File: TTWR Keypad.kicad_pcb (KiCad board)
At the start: 4 copper layers, 35.5 x 60 mm, 46 parts, among them J1 Conn_01x15, J2 Conn_01x15, U1 PTS526 SK15 SMTR2 LFS, U10 PTS526 SK15 SMTR2 LFS, U11 PTS526 SK15 SMTR2 LFS, U12 PTS526 SK15 SMTR2 LFS, U13 PTS526 SK15 SMTR2 LFS, U14 PTS526 SK15 SMTR2 LFS, U15 PTS526 SK15 SMTR2 LFS, U16 PTS526 SK15 SMTR2 LFS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

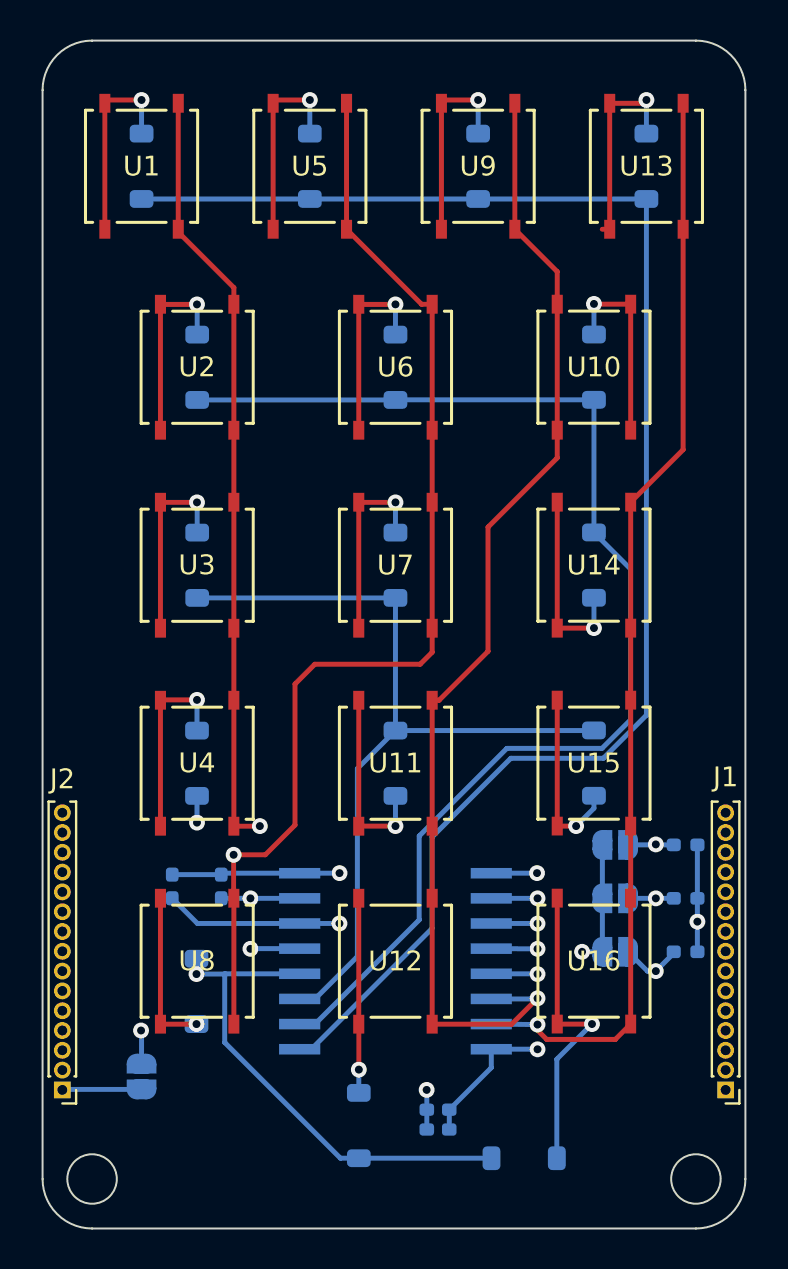
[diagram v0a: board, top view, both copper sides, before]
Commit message: Changed footprints of R* and C* to 0603 and made layout adjustments to compensate. Added JLCPCB metafiles for fab and population.
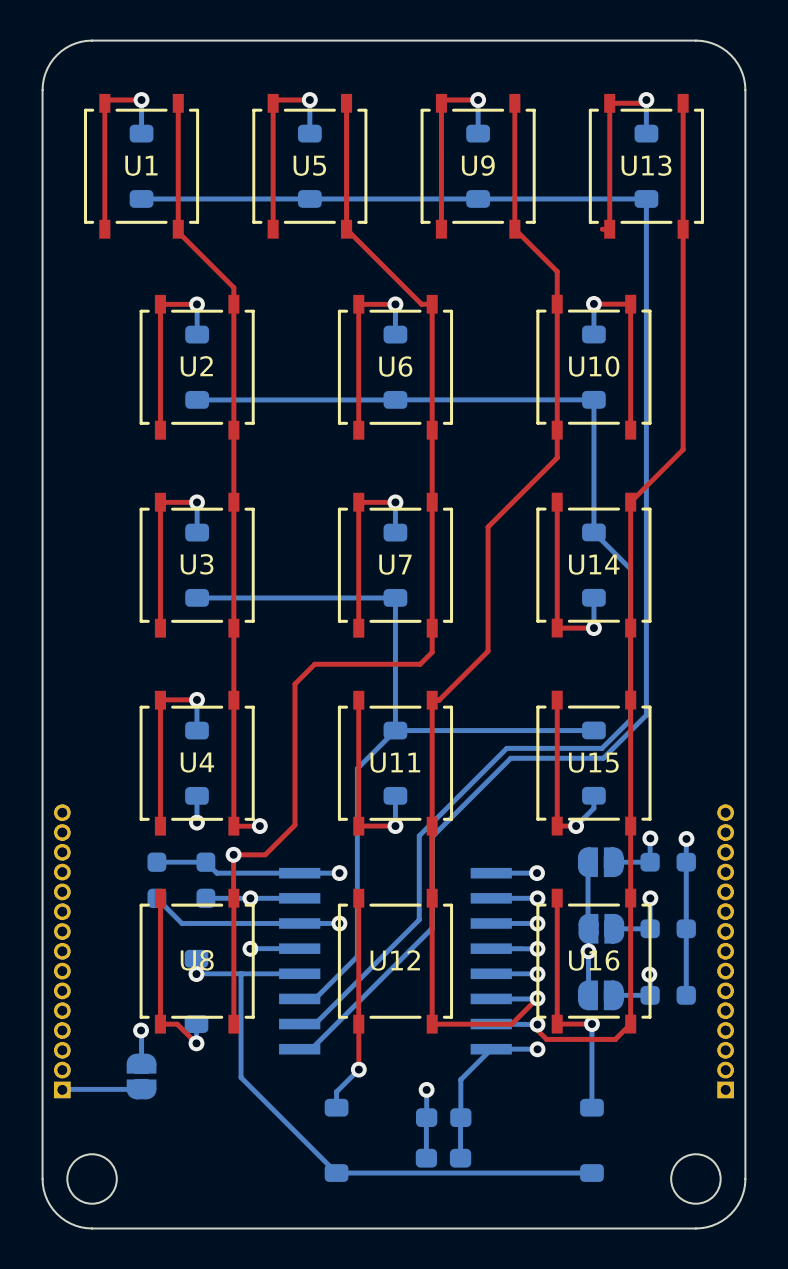
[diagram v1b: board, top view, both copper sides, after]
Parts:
- C1, C2: footprint Capacitor_SMD:C_0402_1005Metric_Pad0.74x0.62mm_HandSolder -> Capacitor_SMD:C_0603_1608Metric_Pad1.08x0.95mm_HandSolder
- J1, J2: moved to B.Cu
- R1, R2, R3, R4, R5: footprint Resistor_SMD:R_0402_1005Metric_Pad0.72x0.64mm_HandSolder -> Resistor_SMD:R_0603_1608Metric_Pad0.98x0.95mm_HandSolder
- moved D16 3.54 mm to (177.8, 95.5), turned to 90 degrees
- moved R5 2.37 mm to (181.6, 88.2)
- moved JP3 2.32 mm to (178.2, 88.2)
- moved R4 1.77 mm to (181.6, 84.9)
- moved JP2 1.69 mm to (178.2, 84.9)
- moved C2 1.48 mm to (170.2, 96.5)
- moved D12 1.35 mm to (164.8, 95.5)
- moved R3 1.24 mm to (181.6, 81.5)
- moved JP1 1.14 mm to (178.2, 81.5)
- moved R1 0.84 mm to (158.2, 82.4)
- moved R2 0.84 mm to (155.8, 82.4)
- moved C1 0.49 mm to (170.3, 94.4)
- turned J1 to 0 degrees
- turned J2 to 0 degrees
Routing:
- net GND: track 32.6 -> 16.4 mm
- net ROW_3: track 34.4 -> 40.0 mm
- net Net-(D16-A): track 15.6 -> 12.3 mm
- net +3.3V: track 52.2 -> 55.0 mm
- net Net-(D8-A): track 8.19 -> 9.56 mm
- net Net-(D12-A): track 9.83 -> 11.0 mm
- net /IO Expander/A1: track 10.7 -> 11.7 mm
- net /IO Expander/SDA: track 33.1 -> 33.9 mm
- net /IO Expander/SCL: track 34.7 -> 35.5 mm
- net /IO Expander/A2: track 12.5 -> 12.0 mm
- added copper zone on In1.Cu, net GND

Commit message: Added ground plane to second inner layer and regenerated gerber files.
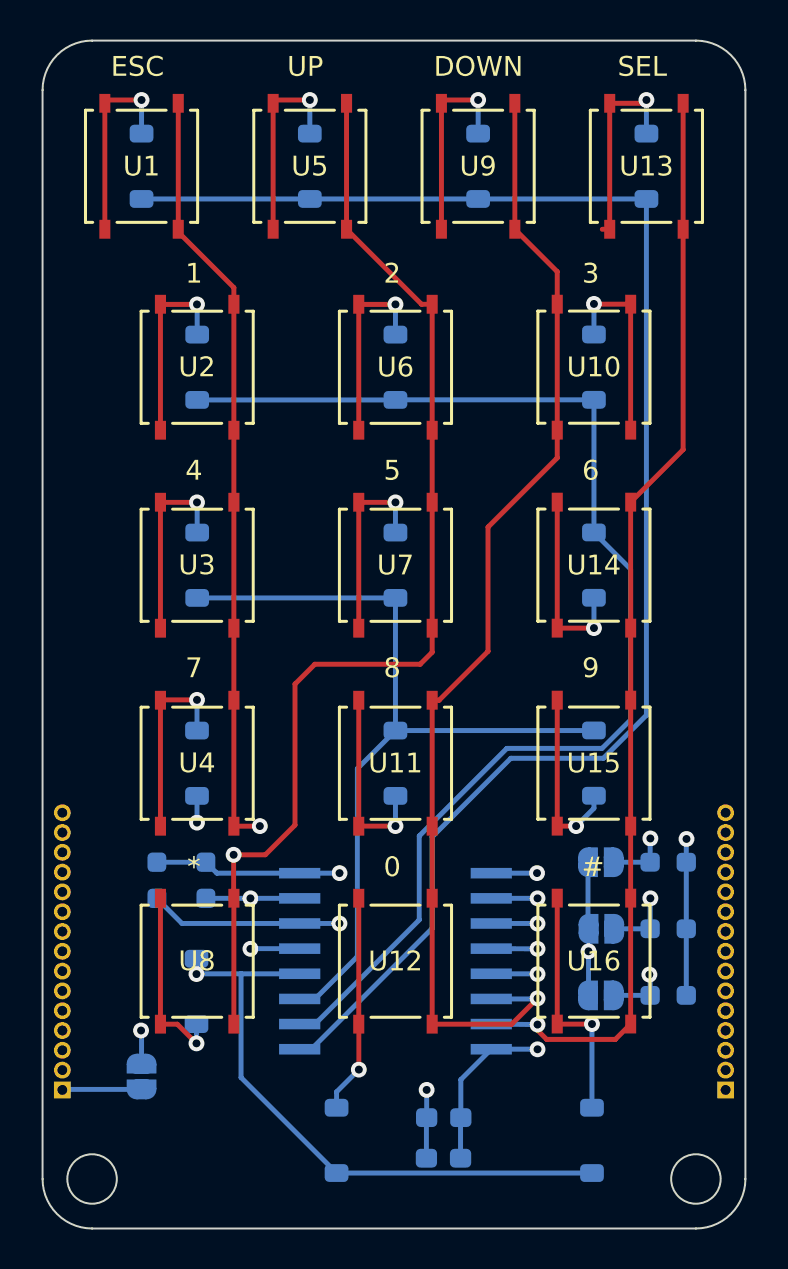
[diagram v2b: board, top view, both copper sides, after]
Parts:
- JP1: value SolderJumper_2_Open -> A0
- JP2: value SolderJumper_2_Open -> A1
- JP3: value SolderJumper_2_Open -> A2
- JP4: value SolderJumper_2_Open -> INT
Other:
- board text added: "#"
- board text added: "*"
- board text added: "0"
- board text added: "1"
- board text added: "2"
- board text added: "3"
- board text added: "4"
- board text added: "5"
- board text added: "6"
- board text added: "7"
- board text added: "8"
- board text added: "9"
- board text added: "DOWN"
- board text added: "ESC"
- board text added: "SEL"
- board text added: "UP"
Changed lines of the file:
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@@
 			(at 0 1.8 90)
 			(layer "B.SilkS")
+			(hide yes)
 			(effects
 				(font
@@
 			)
 		)
-		(property "Value" "SolderJumper_2_Open"
+		(property "Value" "INT"
 			(at 0 -1.9 90)
-			(layer "B.Fab")
-			(hide yes)
+			(layer "B.SilkS")
 			(effects
 				(font
@@
 		(sheetname "IO Expander")
 		(sheetfile "IO Expander.kicad_sch")
-		(attr exclude_from_pos_files)
+		(attr exclude_from_pos_files exclude_from_bom)
 		(fp_line
 			(start -0.7 1)
@@
 			(at -2.35 0 90)
 			(layer "B.SilkS")
+			(hide yes)
 			(effects
 				(font
@@
 			)
 		)
-		(property "Value" "SolderJumper_2_Open"
-			(at 0 -1.9 0)
-			(layer "B.Fab")
-			(hide yes)
+		(property "Value" "A2"
+			(at -2.325 0 -90)
+			(layer "B.SilkS")
 			(effects
 				(font
@@
 		(sheetname "IO Expander")
 		(sheetfile "IO Expander.kicad_sch")
-		(attr exclude_from_pos_files)
+		(attr exclude_from_pos_files exclude_from_bom)
 		(fp_line
 			(start -1.4 -0.3)
@@
 			(at -2.35 0 90)
 			(layer "B.SilkS")
+			(hide yes)
 			(effects
 				(font
@@
 			)
 		)
-		(property "Value" "SolderJumper_2_Open"
-			(at 0 -1.9 0)
-			(layer "B.Fab")
-			(hide yes)
+		(property "Value" "A0"
+			(at -2.325 0.025 -90)
+			(layer "B.SilkS")
 			(effects
 				(font
@@
 		(sheetname "IO Expander")
 		(sheetfile "IO Expander.kicad_sch")
-		(attr exclude_from_pos_files)
+		(attr exclude_from_pos_files exclude_from_bom)
 		(fp_line
 			(start -1.4 -0.3)
@@
 		(sheetname "IO Expander")
 		(sheetfile "IO Expander.kicad_sch")
-		(attr through_hole exclude_from_bom)
+		(attr through_hole exclude_from_pos_files exclude_from_bom)
 		(fp_line
 			(start -0.695 -14.56)
@@
 		(sheetname "IO Expander")
 		(sheetfile "IO Expander.kicad_sch")
-		(attr through_hole exclude_from_bom)
+		(attr through_hole exclude_from_pos_files exclude_from_bom)
 		(fp_line
 			(start -0.695 -14.56)
@@
 			(at -2.35 0 90)
 			(layer "B.SilkS")
+			(hide yes)
 			(effects
 				(font
@@
 			)
 		)
-		(property "Value" "SolderJumper_2_Open"
-			(at 0 -1.9 0)
-			(layer "B.Fab")
-			(hide yes)
+		(property "Value" "A1"
+			(at -2.35 0.0125 -90)
+			(layer "B.SilkS")
 			(effects
 				(font
@@
 		(sheetname "IO Expander")
 		(sheetfile "IO Expander.kicad_sch")
-		(attr exclude_from_pos_files)
+		(attr exclude_from_pos_files exclude_from_bom)
 		(fp_line
 			(start -1.4 -0.3)
@@
 		(layer "Edge.Cuts")
 	)
+	(gr_text "#"
+		(at 177.225 82.325 0)
+		(layer "F.SilkS")
+		(effects
+			(font
+				(size 1 1)
+				(thickness 0.15)
+			)
+			(justify left bottom)
+		)
+	)
+	(gr_text "*"
+		(at 157.303048 82.325 0)
+		(layer "F.SilkS")
+		(effects
+			(font
+				(size 1 1)
+				(thickness 0.15)
+			)
+			(justify left bottom)
+		)
+	)
+	(gr_text "5"
+		(at 167.22381 62.3 0)
+		(layer "F.SilkS")
+		(effects
+			(font
+				(size 1 1)
+				(thickness 0.15)
+			)
+			(justify left bottom)
+		)
+	)
+	(gr_text "8"
+		(at 167.22381 72.275 0)
+		(layer "F.SilkS")
+		(effects
+			(font
+				(size 1 1)
+				(thickness 0.15)
+			)
+			(justify left bottom)
+		)
+	)
+	(gr_text "6"
+		(at 177.24881 62.3 0)
+		(layer "F.SilkS")
+		(effects
+			(font
+				(size 1 1)
+				(thickness 0.15)
+			)
+			(justify left bottom)
+		)
+	)
+	(gr_text "ESC"
+		(at 153.446429 41.9 0)
+		(layer "F.SilkS")
+		(effects
+			(font
+				(size 1 1)
+				(thickness 0.15)
+			)
+			(justify left bottom)
+		)
+	)
+	(gr_text "UP"
+		(at 162.351191 41.9 0)
+		(layer "F.SilkS")
+		(effects
+			(font
+				(size 1 1)
+				(thickness 0.15)
+			)
+			(justify left bottom)
+		)
+	)
+	(gr_text "2"
+		(at 167.22381 52.35 0)
+		(layer "F.SilkS")
+		(effects
+			(font
+				(size 1 1)
+				(thickness 0.15)
+			)
+			(justify left bottom)
+		)
+	)
+	(gr_text "DOWN"
+		(at 169.755953 41.9 0)
+		(layer "F.SilkS")
+		(effects
+			(font
+				(size 1 1)
+				(thickness 0.15)
+			)
+			(justify left bottom)
+		)
+	)
+	(gr_text "0"
+		(at 167.22381 82.325 0)
+		(layer "F.SilkS")
+		(effects
+			(font
+				(size 1 1)
+				(thickness 0.15)
+			)
+			(justify left bottom)
+		)
+	)
+	(gr_text "7"
+		(at 157.20781 72.275 0)
+		(layer "F.SilkS")
+		(effects
+			(font
+				(size 1 1)
+				(thickness 0.15)
+			)
+			(justify left bottom)
+		)
+	)
+	(gr_text "4"
+		(at 157.20781 62.3 0)
+		(layer "F.SilkS")
+		(effects
+			(font
+				(size 1 1)
+				(thickness 0.15)
+			)
+			(justify left bottom)
+		)
+	)
+	(gr_text "1"
+		(at 157.20781 52.35 0)
+		(layer "F.SilkS")
+		(effects
+			(font
+				(size 1 1)
+				(thickness 0.15)
+			)
+			(justify left bottom)
+		)
+	)
+	(gr_text "SEL"
+		(at 179.041667 41.9 0)
+		(layer "F.SilkS")
+		(effects
+			(font
+				(size 1 1)
+				(thickness 0.15)
+			)
+			(justify left bottom)
+		)
+	)
+	(gr_text "9"
+		(at 177.24881 72.275 0)
+		(layer "F.SilkS")
+		(effects
+			(font
+				(size 1 1)
+				(thickness 0.15)
+			)
+			(justify left bottom)
+		)
+	)
+	(gr_text "3"
+		(at 177.24881 52.35 0)
+		(layer "F.SilkS")
+		(effects
+			(font
+				(size 1 1)
+				(thickness 0.15)
+			)
+			(justify left bottom)
+		)
+	)
 	(segment
